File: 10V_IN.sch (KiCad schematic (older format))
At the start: 5 parts, among them U3 LM321

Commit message: Comments and Notation for clarity
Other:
- note added: "1st Order Low Pass Filter"
- note added: "Voltage Divider"
- note added: "Voltage Follower"
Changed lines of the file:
@@
 AR Path="/60A68B69/60A952AD" Ref="R?"  Part="1"
 AR Path="/60A8EFC5/60A952AD" Ref="R5"  Part="1"
-F 0 "R5" V 4495 3600 50  0000 C CNN
-F 1 "22k" V 4586 3600 50  0000 C CNN
+F 0 "R5" V 4500 3600 50  0000 C CNN
+F 1 "22k" V 4600 3600 50  0000 C CNN
 F 2 "" V 4740 3590 50  0001 C CNN
 F 3 "~" H 4700 3600 50  0001 C CNN
@@
 AR Path="/60A68B69/60A952C7" Ref="U?"  Part="1"
 AR Path="/60A8EFC5/60A952C7" Ref="U3"  Part="1"
-F 0 "U3" H 6044 3746 50  0000 L CNN
-F 1 "LM321" H 6044 3655 50  0000 L CNN
+F 0 "U3" H 5800 3600 50  0000 L CNN
+F 1 "LM321" H 5800 3500 50  0000 L CNN
 F 2 "Package_TO_SOT_SMD:SOT-23-5" H 5700 3700 50  0001 C CNN
 F 3 "http://www.ti.com/lit/ds/symlink/lm321.pdf" H 5700 3700 50  0001 C CNN
@@
 Wire Wire Line
 	5050 3800 5050 3600
-Text HLabel 7000 3700 2    50   Input ~ 0
+Text HLabel 7300 3700 2    50   Input ~ 0
 OUT
 Text GLabel 5800 4150 2    50   Input ~ 0
@@
 AR Path="/60A68B69/60A9BABC" Ref="R?"  Part="1"
 AR Path="/60A8EFC5/60A9BABC" Ref="R7"  Part="1"
-F 0 "R7" V 6295 3700 50  0000 C CNN
-F 1 "2.2k" V 6386 3700 50  0000 C CNN
+F 0 "R7" V 6300 3700 50  0000 C CNN
+F 1 "2.2k" V 6400 3700 50  0000 C CNN
 F 2 "" V 6540 3690 50  0001 C CNN
 F 3 "~" H 6500 3700 50  0001 C CNN
@@
 Wire Wire Line
 	6850 3800 6850 3700
-Connection ~ 6850 3700
-Wire Wire Line
-	6850 3700 7000 3700
 Wire Wire Line
 	6150 3700 6350 3700
@@
 	6150 4300 6850 4300
 Connection ~ 6150 4300
+Wire Notes Line
+	4100 3350 5300 3350
+Wire Notes Line
+	5300 3350 5300 4400
+Wire Notes Line
+	5300 4400 4100 4400
+Wire Notes Line
+	4100 4400 4100 3350
+Text Notes 5000 4500 2    50   ~ 0
+Voltage Divider
+Wire Notes Line
+	5350 3150 6300 3150
+Wire Notes Line
+	6300 3150 6300 4400
+Wire Notes Line
+	6300 4400 5350 4400
+Wire Notes Line
+	5350 4400 5350 3150
+Wire Wire Line
+	6850 3700 7300 3700
+Connection ~ 6850 3700
+Wire Notes Line
+	6350 3450 6350 4400
+Wire Notes Line
+	6350 4400 7250 4400
+Wire Notes Line
+	7250 4400 7250 3450
+Wire Notes Line
+	7250 3450 6350 3450
+Text Notes 6150 4500 2    50   ~ 0
+Voltage Follower
+Text Notes 7300 4500 2    50   ~ 0
+1st Order Low Pass Filter
 $EndSCHEMATC

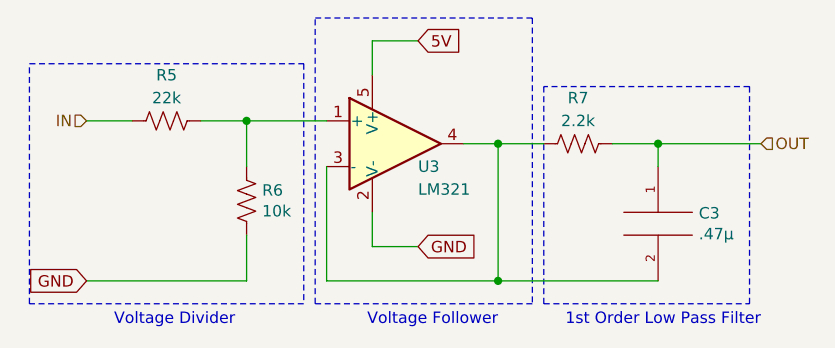
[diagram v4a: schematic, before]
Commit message: Footprint Association
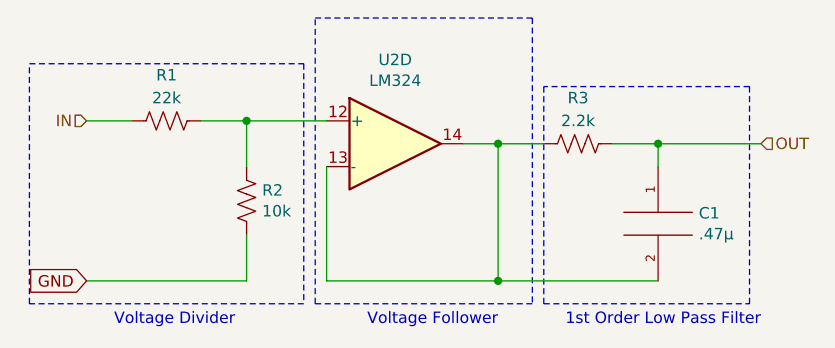
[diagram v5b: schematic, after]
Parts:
- removed U3: LM321, Package_TO_SOT_SMD:SOT-23-5, symbol Amplifier_Operational:LM321
- added U2: LM324, Package_DIP:DIP-14_W7.62mm, symbol Amplifier_Operational:LM324
- C1: renamed from C3; footprint (none) -> Capacitor_THT:C_Disc_D5.1mm_W3.2mm_P5.00mm
- R1: renamed from R5; footprint (none) -> Resistor_THT:R_Axial_DIN0207_L6.3mm_D2.5mm_P10.16mm_Horizontal
- R2: renamed from R6; footprint (none) -> Resistor_THT:R_Axial_DIN0207_L6.3mm_D2.5mm_P10.16mm_Horizontal
- R3: renamed from R7; footprint (none) -> Resistor_THT:R_Axial_DIN0207_L6.3mm_D2.5mm_P10.16mm_Horizontal
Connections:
- net at R1.1, R2.2: now also U2.12 (+)
- net at C1.2, R3.2: now also U2.13 (-), U2.14
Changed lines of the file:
@@
 P 4700 3600
 AR Path="/60A68B69/60A952AD" Ref="R?"  Part="1"
-AR Path="/60A8EFC5/60A952AD" Ref="R5"  Part="1"
-F 0 "R5" V 4500 3600 50  0000 C CNN
+AR Path="/60A8EFC5/60A952AD" Ref="R1"  Part="1"
+F 0 "R1" V 4500 3600 50  0000 C CNN
 F 1 "22k" V 4600 3600 50  0000 C CNN
-F 2 "" V 4740 3590 50  0001 C CNN
+F 2 "Resistor_THT:R_Axial_DIN0207_L6.3mm_D2.5mm_P10.16mm_Horizontal" V 4740 3590 50  0001 C CNN
 F 3 "~" H 4700 3600 50  0001 C CNN
 	1    4700 3600
@@
 Text GLabel 4350 4300 0    50   Input ~ 0
 GND
-$Comp
-L Amplifier_Operational:LM321 U?
-U 1 1 60A952C7
-P 5700 3700
-AR Path="/60A68B69/60A952C7" Ref="U?"  Part="1"
-AR Path="/60A8EFC5/60A952C7" Ref="U3"  Part="1"
-F 0 "U3" H 5800 3600 50  0000 L CNN
-F 1 "LM321" H 5800 3500 50  0000 L CNN
-F 2 "Package_TO_SOT_SMD:SOT-23-5" H 5700 3700 50  0001 C CNN
-F 3 "http://www.ti.com/lit/ds/symlink/lm321.pdf" H 5700 3700 50  0001 C CNN
-	1    5700 3700
-	1    0    0    -1
-$EndComp
 Wire Wire Line
 	4350 3600 4550 3600
@@
 Text HLabel 7300 3700 2    50   Input ~ 0
 OUT
-Text GLabel 5800 4150 2    50   Input ~ 0
-GND
-Wire Wire Line
-	5600 4000 5600 4150
-Wire Wire Line
-	5600 4150 5800 4150
-Wire Wire Line
-	5600 3400 5600 3250
-Wire Wire Line
-	5600 3250 5800 3250
 Text HLabel 4350 3600 0    50   Input ~ 0
 IN
@@
 P 5050 3950
 AR Path="/60A68B69/60A98D5B" Ref="R?"  Part="1"
-AR Path="/60A8EFC5/60A98D5B" Ref="R6"  Part="1"
-F 0 "R6" H 4982 3904 50  0000 R CNN
+AR Path="/60A8EFC5/60A98D5B" Ref="R2"  Part="1"
+F 0 "R2" H 4982 3904 50  0000 R CNN
 F 1 "10k" H 4982 3995 50  0000 R CNN
-F 2 "" V 5090 3940 50  0001 C CNN
+F 2 "Resistor_THT:R_Axial_DIN0207_L6.3mm_D2.5mm_P10.16mm_Horizontal" V 5090 3940 50  0001 C CNN
 F 3 "~" H 5050 3950 50  0001 C CNN
 	1    5050 3950
@@
 Wire Wire Line
 	6000 3700 6150 3700
-Text GLabel 5800 3250 2    50   Input ~ 0
-5V
 Wire Wire Line
 	6150 3700 6150 4300
@@
 P 6500 3700
 AR Path="/60A68B69/60A9BABC" Ref="R?"  Part="1"
-AR Path="/60A8EFC5/60A9BABC" Ref="R7"  Part="1"
-F 0 "R7" V 6300 3700 50  0000 C CNN
+AR Path="/60A8EFC5/60A9BABC" Ref="R3"  Part="1"
+F 0 "R3" V 6300 3700 50  0000 C CNN
 F 1 "2.2k" V 6400 3700 50  0000 C CNN
-F 2 "" V 6540 3690 50  0001 C CNN
+F 2 "Resistor_THT:R_Axial_DIN0207_L6.3mm_D2.5mm_P10.16mm_Horizontal" V 6540 3690 50  0001 C CNN
 F 3 "~" H 6500 3700 50  0001 C CNN
 	1    6500 3700
@@
 $EndComp
 $Comp
-L pspice:CAP C3
+L pspice:CAP C1
 U 1 1 60A9C9D5
 P 6850 4050
-F 0 "C3" H 7028 4096 50  0000 L CNN
+F 0 "C1" H 7028 4096 50  0000 L CNN
 F 1 ".47μ" H 7028 4005 50  0000 L CNN
-F 2 "" H 6850 4050 50  0001 C CNN
+F 2 "Capacitor_THT:C_Disc_D5.1mm_W3.2mm_P5.00mm" H 6850 4050 50  0001 C CNN
 F 3 "~" H 6850 4050 50  0001 C CNN
 	1    6850 4050
@@
 Text Notes 7300 4500 2    50   ~ 0
 1st Order Low Pass Filter
+$Comp
+L Amplifier_Operational:LM324 U2
+U 4 1 60C68302
+P 5700 3700
+F 0 "U2" H 5700 4067 50  0000 C CNN
+F 1 "LM324" H 5700 3976 50  0000 C CNN
+F 2 "Package_DIP:DIP-14_W7.62mm" H 5650 3800 50  0001 C CNN
+F 3 "http://www.ti.com/lit/ds/symlink/lm2902-n.pdf" H 5750 3900 50  0001 C CNN
+	4    5700 3700
+	1    0    0    -1
+$EndComp
 $EndSCHEMATC

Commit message: Fixed a couple of discrepancies between my test circuit and the schematic
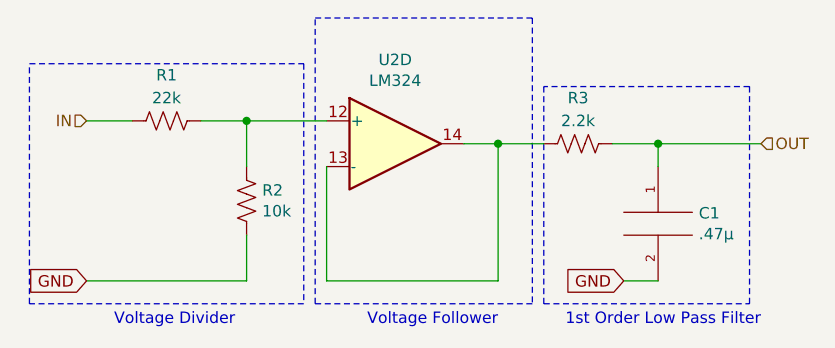
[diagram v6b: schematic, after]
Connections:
- net GND: now also C1.2
- net at R3.2, U2.13 (-), U2.14: no longer C1.2
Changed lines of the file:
@@
 	6150 3700 6350 3700
 Connection ~ 6150 3700
-Wire Wire Line
-	6150 4300 6850 4300
-Connection ~ 6150 4300
 Wire Notes Line
 	4100 3350 5300 3350
@@
 	1    0    0    -1
 $EndComp
+Text GLabel 6700 4300 0    50   Input ~ 0
+GND
+Wire Wire Line
+	6850 4300 6700 4300
 $EndSCHEMATC
